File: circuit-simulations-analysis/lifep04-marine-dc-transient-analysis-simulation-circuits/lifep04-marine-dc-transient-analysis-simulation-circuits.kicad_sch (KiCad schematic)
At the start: 17 parts

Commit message: Remove accidental embedded repo and ignore .history
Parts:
- C2_interwinding_capacitance1: value 5nF -> 5n
- renumbered D1_motor_flyback to D1_motor_flyback1
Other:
- note added: "April 2026"
- note added: "Lifep04-marine-dc-transient-analysis-simulation"
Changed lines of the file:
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@@
+		)
+	)
+	(text "Lifep04-marine-dc-transient-analysis-simulation"
+		(exclude_from_sim no)
+		(at 212.344 189.738 0)
+		(effects
+			(font
+				(size 1.27 1.27)
+			)
+		)
+	)
+	(text "April 2026"
+		(exclude_from_sim no)
+		(at 211.836 193.548 0)
+		(effects
+			(font
+				(size 1.27 1.27)
+			)
 		)
 	)
@@
 		)
 		(instances
-			(project "liefp04-marine-dc-transient-analysis-simulation-circuits"
+			(project "lifep04-marine-dc-transient-analysis-simulation-circuits"
 				(path "/8ee89d25-0260-4689-a3bc-2207fab472f1"
 					(reference "#PWR01")
@@
 		)
 		(instances
-			(project "liefp04-marine-dc-transient-analysis-simulation-circuits"
+			(project "lifep04-marine-dc-transient-analysis-simulation-circuits"
 				(path "/8ee89d25-0260-4689-a3bc-2207fab472f1"
 					(reference "R5_magnetic_loss1")
@@
 		)
 		(instances
-			(project "liefp04-marine-dc-transient-analysis-simulation-circuits"
+			(project "lifep04-marine-dc-transient-analysis-simulation-circuits"
 				(path "/8ee89d25-0260-4689-a3bc-2207fab472f1"
 					(reference "LifeP04-4s2P1")
@@
 		)
 		(instances
-			(project "liefp04-marine-dc-transient-analysis-simulation-circuits"
+			(project "lifep04-marine-dc-transient-analysis-simulation-circuits"
 				(path "/8ee89d25-0260-4689-a3bc-2207fab472f1"
 					(reference "L5_motor_inductance1")
@@
 		)
 		(instances
-			(project "liefp04-marine-dc-transient-analysis-simulation-circuits"
+			(project "lifep04-marine-dc-transient-analysis-simulation-circuits"
 				(path "/8ee89d25-0260-4689-a3bc-2207fab472f1"
 					(reference "C3")
@@
 		)
 		(instances
-			(project "liefp04-marine-dc-transient-analysis-simulation-circuits"
+			(project "lifep04-marine-dc-transient-analysis-simulation-circuits"
 				(path "/8ee89d25-0260-4689-a3bc-2207fab472f1"
 					(reference "L1_batt1")
@@
 		)
 		(instances
-			(project "liefp04-marine-dc-transient-analysis-simulation-circuits"
+			(project "lifep04-marine-dc-transient-analysis-simulation-circuits"
 				(path "/8ee89d25-0260-4689-a3bc-2207fab472f1"
 					(reference "R1_batt_dc_internal1")
@@
 		)
 		(instances
-			(project "liefp04-marine-dc-transient-analysis-simulation-circuits"
+			(project "lifep04-marine-dc-transient-analysis-simulation-circuits"
 				(path "/8ee89d25-0260-4689-a3bc-2207fab472f1"
 					(reference "R4_cable_loop_resistance1")
@@
 			)
 		)
-		(property "Value" "5nF"
+		(property "Value" "5n"
 			(at 211.328 115.57 0)
 			(show_name no)
@@
 			)
 		)
+		(property "Sim.Device" "C"
+			(at 0 0 0)
+			(hide yes)
+			(show_name no)
+			(do_not_autoplace no)
+			(effects
+				(font
+					(size 1.27 1.27)
+				)
+			)
+		)
+		(property "Sim.Pins" "1=+ 2=-"
+			(at 0 0 0)
+			(hide yes)
+			(show_name no)
+			(do_not_autoplace no)
+			(effects
+				(font
+					(size 1.27 1.27)
+				)
+			)
+		)
 		(pin "2"
 		)
@@
 		)
 		(instances
-			(project "liefp04-marine-dc-transient-analysis-simulation-circuits"
+			(project "lifep04-marine-dc-transient-analysis-simulation-circuits"
 				(path "/8ee89d25-0260-4689-a3bc-2207fab472f1"
 					(reference "C2_interwinding_capacitance1")
@@
 			)
 		)
-		(property "Sim.Params" "y1=0 y2=12 td=5m tr=2n tf=2n tw=5m per=10m"
+		(property "Sim.Params" "y1=0 y2=12 td=5m tr=2n tf=2n tw=25m per=100m"
 			(at 162.4302 44.45 90)
 			(show_name no)
@@
 		)
 		(instances
-			(project "liefp04-marine-dc-transient-analysis-simulation-circuits"
+			(project "lifep04-marine-dc-transient-analysis-simulation-circuits"
 				(path "/8ee89d25-0260-4689-a3bc-2207fab472f1"
 					(reference "V1")
@@
 		)
 		(instances
-			(project "liefp04-marine-dc-transient-analysis-simulation-circuits"
+			(project "lifep04-marine-dc-transient-analysis-simulation-circuits"
 				(path "/8ee89d25-0260-4689-a3bc-2207fab472f1"
 					(reference "L4_relay_drive_coil1")
@@
 		)
 		(instances
-			(project "liefp04-marine-dc-transient-analysis-simulation-circuits"
+			(project "lifep04-marine-dc-transient-analysis-simulation-circuits"
 				(path "/8ee89d25-0260-4689-a3bc-2207fab472f1"
 					(reference "R2_bat_losses1")
@@
 		)
 		(instances
-			(project "liefp04-marine-dc-transient-analysis-simulation-circuits"
+			(project "lifep04-marine-dc-transient-analysis-simulation-circuits"
 				(path "/8ee89d25-0260-4689-a3bc-2207fab472f1"
 					(reference "R3_fuse-class_t1")
@@
 		)
 		(instances
-			(project "liefp04-marine-dc-transient-analysis-simulation-circuits"
+			(project "lifep04-marine-dc-transient-analysis-simulation-circuits"
 				(path "/8ee89d25-0260-4689-a3bc-2207fab472f1"
 					(reference "L2_cable_loop_inductance1")
@@
 		)
 		(instances
-			(project "liefp04-marine-dc-transient-analysis-simulation-circuits"
+			(project "lifep04-marine-dc-transient-analysis-simulation-circuits"
 				(path "/8ee89d25-0260-4689-a3bc-2207fab472f1"
 					(reference "R6_motor_winding1")
@@
 		)
 		(instances
-			(project "liefp04-marine-dc-transient-analysis-simulation-circuits"
+			(project "lifep04-marine-dc-transient-analysis-simulation-circuits"
 				(path "/8ee89d25-0260-4689-a3bc-2207fab472f1"
 					(reference "C1")
@@
 		)
 		(instances
-			(project "liefp04-marine-dc-transient-analysis-simulation-circuits"
+			(project "lifep04-marine-dc-transient-analysis-simulation-circuits"
 				(path "/8ee89d25-0260-4689-a3bc-2207fab472f1"
 					(reference "#PWR02")
@@
 		)
 		(instances
-			(project "liefp04-marine-dc-transient-analysis-simulation-circuits"
+			(project "lifep04-marine-dc-transient-analysis-simulation-circuits"
 				(path "/8ee89d25-0260-4689-a3bc-2207fab472f1"
 					(reference "S1")
@@
 		(in_pos_files yes)
 		(dnp no)
-		(property "Reference" "D1_motor_flyback"
+		(property "Reference" "D1_motor_flyback1"
 			(at 240.284 114.3 0)
 			(show_name no)
@@
 		)
 		(instances
-			(project "liefp04-marine-dc-transient-analysis-simulation-circuits"
+			(project "lifep04-marine-dc-transient-analysis-simulation-circuits"
 				(path "/8ee89d25-0260-4689-a3bc-2207fab472f1"
-					(reference "D1_motor_flyback")
+					(reference "D1_motor_flyback1")
 					(unit 1)
 				)

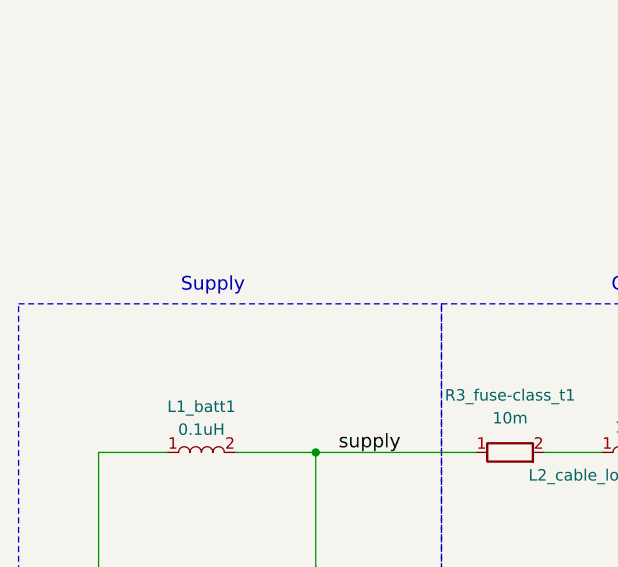
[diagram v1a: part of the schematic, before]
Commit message: updates to file structures
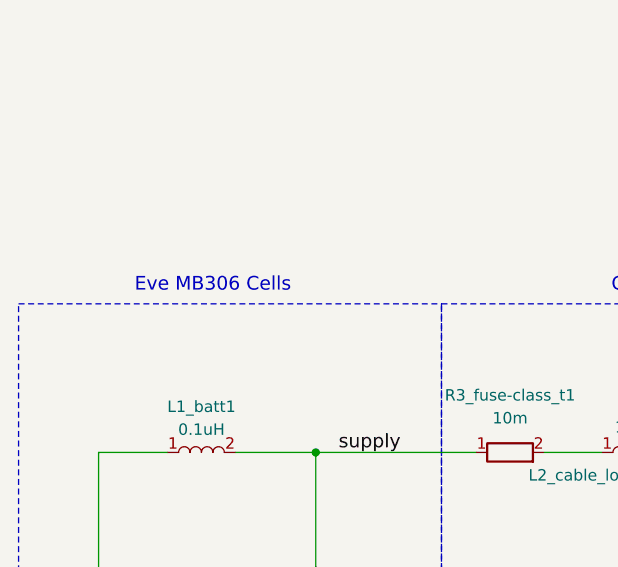
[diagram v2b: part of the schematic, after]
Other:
- note added: "Eve MB306 Cells"
- note removed: "Supply"
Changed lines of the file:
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@@
 		)
 	)
-	(text "Supply"
+	(text "Eve MB306 Cells"
 		(exclude_from_sim no)
 		(at 64.77 74.168 0)

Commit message: updates to images
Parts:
- removed V1: VPULSE, symbol Simulation_SPICE:VPULSE
- added V2: VPWL, symbol Simulation_SPICE:VPWL
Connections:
- net GND: now also V2.2
- net relay: no longer names the net of C3.1, L4_relay_drive_coil1.1
- net relay: now also V2.1
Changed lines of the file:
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@@
 	)
 	(label "relay"
-		(at 146.05 49.53 0)
+		(at 170.18 49.53 0)
 		(effects
 			(font
@@
 	)
 	(symbol
-		(lib_id "Simulation_SPICE:VPULSE")
-		(at 162.56 49.53 90)
-		(unit 1)
-		(body_style 1)
-		(exclude_from_sim no)
-		(in_bom yes)
-		(on_board yes)
-		(in_pos_files yes)
-		(dnp no)
-		(fields_autoplaced yes)
-		(property "Reference" "V1"
-			(at 162.4302 39.37 90)
-			(show_name no)
-			(do_not_autoplace no)
-			(effects
-				(font
-					(size 1.27 1.27)
-				)
-			)
-		)
-		(property "Value" "VPULSE"
-			(at 162.4302 41.91 90)
-			(show_name no)
-			(do_not_autoplace no)
-			(effects
-				(font
-					(size 1.27 1.27)
-				)
-			)
-		)
-		(property "Footprint" ""
-			(at 162.56 49.53 0)
-			(hide yes)
-			(show_name no)
-			(do_not_autoplace no)
-			(effects
-				(font
-					(size 1.27 1.27)
-				)
-			)
-		)
-		(property "Datasheet" "https://ngspice.sourceforge.io/docs/ngspice-html-manual/manual.xhtml#sec_Independent_Sources_for"
-			(at 162.56 49.53 0)
-			(hide yes)
-			(show_name no)
-			(do_not_autoplace no)
-			(effects
-				(font
-					(size 1.27 1.27)
-				)
-			)
-		)
-		(property "Description" "Voltage source, pulse"
-			(at 162.56 49.53 0)
-			(hide yes)
-			(show_name no)
-			(do_not_autoplace no)
-			(effects
-				(font
-					(size 1.27 1.27)
-				)
-			)
-		)
-		(property "Sim.Pins" "1=+ 2=-"
-			(at 162.56 49.53 0)
-			(hide yes)
-			(show_name no)
-			(do_not_autoplace no)
-			(effects
-				(font
-					(size 1.27 1.27)
-				)
-			)
-		)
-		(property "Sim.Type" "PULSE"
-			(at 162.56 49.53 0)
-			(hide yes)
-			(show_name no)
-			(do_not_autoplace no)
-			(effects
-				(font
-					(size 1.27 1.27)
-				)
-			)
-		)
-		(property "Sim.Device" "V"
-			(at 162.56 49.53 0)
-			(hide yes)
-			(show_name no)
-			(do_not_autoplace no)
-			(effects
-				(font
-					(size 1.27 1.27)
-				)
-				(justify left)
-			)
-		)
-		(property "Sim.Params" "y1=0 y2=12 td=5m tr=2n tf=2n tw=25m per=100m"
-			(at 162.4302 44.45 90)
-			(show_name no)
-			(do_not_autoplace no)
-			(effects
-				(font
-					(size 1.27 1.27)
-				)
-			)
-		)
-		(pin "1"
-		)
-		(pin "2"
-		)
-		(instances
-			(project "lifep04-marine-dc-transient-analysis-simulation-circuits"
-				(path "/8ee89d25-0260-4689-a3bc-2207fab472f1"
-					(reference "V1")
-					(unit 1)
-				)
-			)
-		)
-	)
-	(symbol
 		(lib_name "L_1")
 		(lib_id "Device:L")
@@
 					(unit 1)
 				)
+			)
+		)
+	)
+	(symbol
+		(lib_id "Simulation_SPICE:VPWL")
+		(at 162.56 49.53 90)
+		(unit 1)
+		(body_style 1)
+		(exclude_from_sim no)
+		(in_bom yes)
+		(on_board yes)
+		(in_pos_files yes)
+		(dnp no)
+		(fields_autoplaced yes)
+		(property "Reference" "V2"
+			(at 162.4302 39.37 90)
+			(show_name no)
+			(do_not_autoplace no)
+			(effects
+				(font
+					(size 1.27 1.27)
+				)
+			)
+		)
+		(property "Value" "VPWL"
+			(at 162.4302 41.91 90)
+			(show_name no)
+			(do_not_autoplace no)
+			(effects
+				(font
+					(size 1.27 1.27)
+				)
+			)
+		)
+		(property "Footprint" ""
+			(at 162.56 49.53 0)
+			(hide yes)
+			(show_name no)
+			(do_not_autoplace no)
+			(effects
+				(font
+					(size 1.27 1.27)
+				)
+			)
+		)
+		(property "Datasheet" "https://ngspice.sourceforge.io/docs/ngspice-html-manual/manual.xhtml#sec_Independent_Sources_for"
+			(at 162.56 49.53 0)
+			(hide yes)
+			(show_name no)
+			(do_not_autoplace no)
+			(effects
+				(font
+					(size 1.27 1.27)
+				)
+			)
+		)
+		(property "Description" "Voltage source, piece-wise linear"
+			(at 162.56 49.53 0)
+			(hide yes)
+			(show_name no)
+			(do_not_autoplace no)
+			(effects
+				(font
+					(size 1.27 1.27)
+				)
+			)
+		)
+		(property "Sim.Pins" "1=+ 2=-"
+			(at 162.56 49.53 0)
+			(hide yes)
+			(show_name no)
+			(do_not_autoplace no)
+			(effects
+				(font
+					(size 1.27 1.27)
+				)
+			)
+		)
+		(property "Sim.Device" "V"
+			(at 162.56 49.53 0)
+			(hide yes)
+			(show_name no)
+			(do_not_autoplace no)
+			(effects
+				(font
+					(size 1.27 1.27)
+				)
+				(justify left)
+			)
+		)
+		(property "Sim.Params" "pwl=\"0 0 20u 0 22u 13 42u 13 44u 0 68u 0 70u 13 96u 13 98u 0 132u 0 134u 13 178u 1 180u 0 238u 0 240u 13 318u 13 320u 0 430u 0 432u 13 575u 13 577u 0 740u 0 742u 13 920u 13 922u 0 990u 0 1m 13 11m 13 11.02m 0 11.055m 0 11.057m 13 11.095m 13 11.097m 0 11.16m 0 11.162m 13 11.21m 13 11.212m 0 11.3m 0 11.302m 13 11.335m 13 11.337m 0 11.47m 0 11.472m 13 11.49m 13 11.492m 0 11.7m 0\""
+			(at 162.4302 44.45 90)
+			(show_name no)
+			(do_not_autoplace no)
+			(effects
+				(font
+					(size 1.27 1.27)
+				)
+			)
+		)
+		(property "Sim.Type" "PWL"
+			(at 162.56 49.53 0)
+			(hide yes)
+			(show_name no)
+			(do_not_autoplace no)
+			(effects
+				(font
+					(size 1.27 1.27)
+				)
+			)
+		)
+		(pin "1"
+		)
+		(pin "2"
+		)
+		(instances
+			(project "lifep04-marine-dc-transient-analysis-simulation-circuits"
+				(path "/8ee89d25-0260-4689-a3bc-2207fab472f1"
+					(reference "V2")
+					(unit 1)
+				)
